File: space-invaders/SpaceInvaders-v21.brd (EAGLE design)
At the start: 91.4 x 91.4 mm, 27 parts, among them J2-J4 TM4C123GXL, J3-J1 TM4C123GXL, J5 NOKIA_5110, J6 NOKIA_5110, J7 9V, U1 LM7805CT

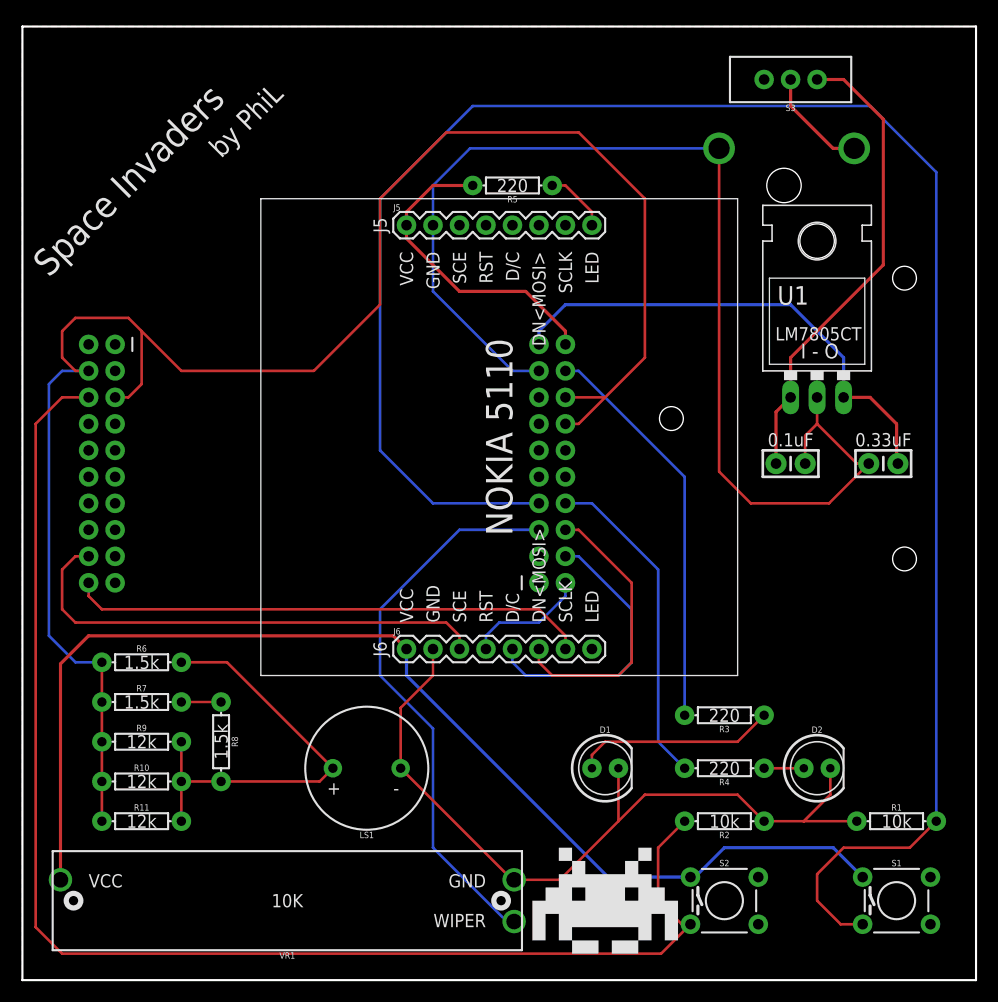
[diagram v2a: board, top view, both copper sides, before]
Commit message: Fillet corners of the boards
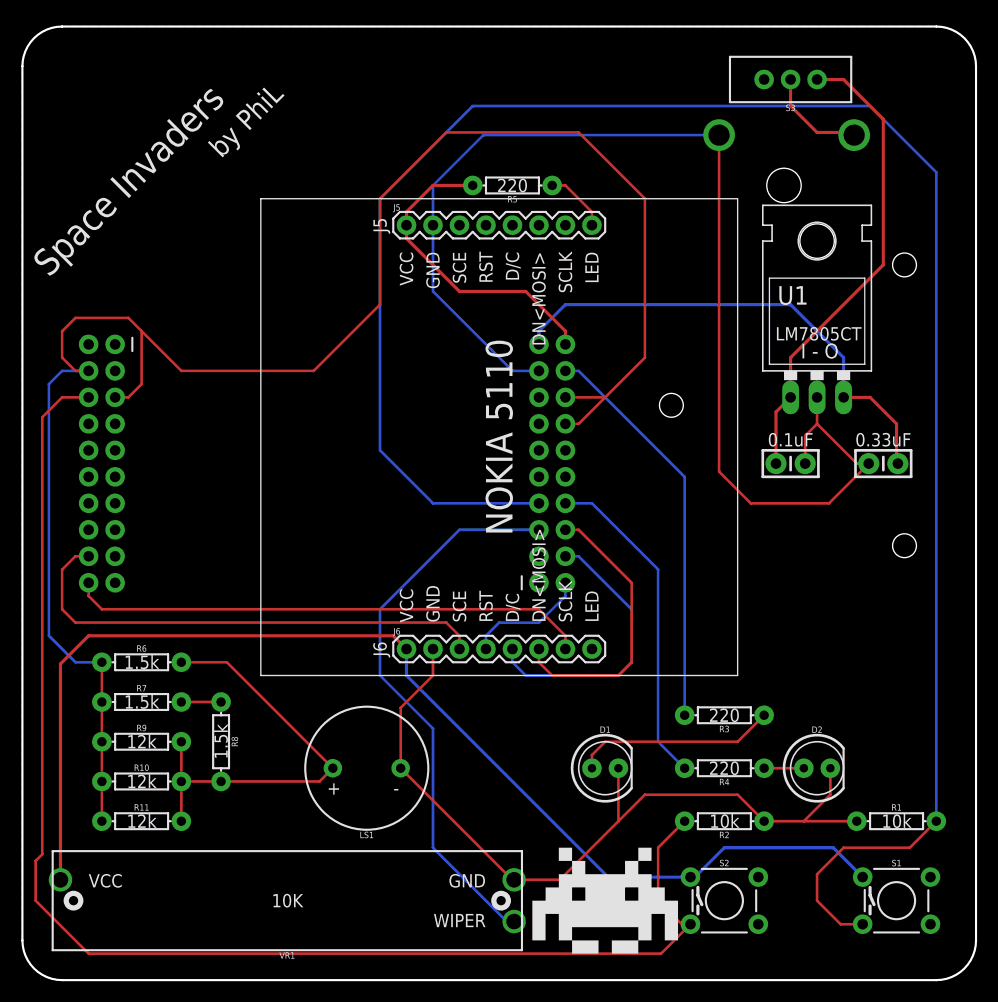
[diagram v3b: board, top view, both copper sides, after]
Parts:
- moved J7 1.27 mm to (58.4, 27.9)
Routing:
- net GND: track 190.4 -> 192.2 mm
- net PE0: track 132.1 -> 130.6 mm
- net VIN: track 10.3 -> 9.79 mm
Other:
- outline, holes or cut-outs redrawn
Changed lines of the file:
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@@
 <board>
 <plain>
-<wire x1="0" y1="0" x2="0" y2="91.44" width="0.2032" layer="20"/>
-<wire x1="0" y1="91.44" x2="91.44" y2="91.44" width="0.2032" layer="20"/>
-<wire x1="91.44" y1="91.44" x2="91.44" y2="0" width="0.2032" layer="20"/>
-<wire x1="91.44" y1="0" x2="0" y2="0" width="0.2032" layer="20"/>
+<wire x1="0" y1="3.81" x2="0" y2="87.63" width="0.2032" layer="20"/>
+<wire x1="3.81" y1="91.44" x2="87.63" y2="91.44" width="0.2032" layer="20"/>
+<wire x1="91.44" y1="87.63" x2="91.44" y2="3.81" width="0.2032" layer="20"/>
+<wire x1="87.63" y1="0" x2="3.81" y2="0" width="0.2032" layer="20"/>
 <wire x1="22.86" y1="74.93" x2="68.58" y2="74.93" width="0.127" layer="21"/>
 <wire x1="68.58" y1="74.93" x2="68.58" y2="29.21" width="0.127" layer="21"/>
@@
 <rectangle x1="52.705" y1="2.54" x2="53.975" y2="3.81" layer="21"/>
 <rectangle x1="51.435" y1="3.81" x2="52.705" y2="5.08" layer="21"/>
+<wire x1="0" y1="87.63" x2="3.81" y2="91.44" width="0.2032" layer="20" curve="-90"/>
+<wire x1="87.63" y1="91.44" x2="91.44" y2="87.63" width="0.2032" layer="20" curve="-90"/>
+<wire x1="91.44" y1="3.81" x2="87.63" y2="0" width="0.2032" layer="20" curve="-90"/>
+<wire x1="0" y1="3.81" x2="3.81" y2="0" width="0.2032" layer="20" curve="90"/>
 </plain>
 <attributes>
@@
 <attribute name="PROD_ID" value="CONN-08438" x="36.83" y="31.75" size="1.778" layer="27" display="off"/>
 </element>
-<element name="J7" library="SparkFun-Connectors" package="BC9VPC" value="9V" x="58.42" y="26.67" rot="MR90">
-<attribute name="PROD_ID" value="BATT-10855" x="58.42" y="26.67" size="1.778" layer="28" rot="MR90" display="off"/>
+<element name="J7" library="SparkFun-Connectors" package="BC9VPC" value="9V" x="58.42" y="27.94" rot="MR90">
+<attribute name="PROD_ID" value="BATT-10855" x="58.42" y="27.94" size="1.778" layer="28" rot="MR90" display="off"/>
 </element>
 <element name="LS1" library="SparkFun-Electromechanical" package="BUZZER-12MM" value="BUZZER" x="33.02" y="20.32" rot="R180">
@@
 <wire x1="47.15" y1="9.62" x2="46.97" y2="9.62" width="0.254" layer="1"/>
 <wire x1="46.97" y1="9.62" x2="36.27" y2="20.32" width="0.254" layer="1"/>
-<wire x1="66.802" y1="79.756" x2="42.926" y2="79.756" width="0.254" layer="16"/>
-<wire x1="42.926" y1="79.756" x2="39.37" y2="76.2" width="0.254" layer="16"/>
-<wire x1="39.37" y1="76.2" x2="39.37" y2="72.39" width="0.254" layer="16"/>
+<wire x1="39.37" y1="72.39" x2="39.37" y2="76.2" width="0.254" layer="16"/>
 <wire x1="39.37" y1="72.39" x2="39.37" y2="66.04" width="0.254" layer="16"/>
 <wire x1="39.37" y1="66.04" x2="46.99" y2="58.42" width="0.254" layer="16"/>
@@
 <wire x1="39.37" y1="29.21" x2="39.37" y2="31.75" width="0.254" layer="1"/>
 <wire x1="36.27" y1="20.32" x2="36.27" y2="26.11" width="0.254" layer="1"/>
-<wire x1="66.802" y1="79.756" x2="66.802" y2="48.768" width="0.254" layer="1"/>
+<wire x1="66.802" y1="81.026" x2="66.802" y2="48.768" width="0.254" layer="1"/>
 <wire x1="66.802" y1="48.768" x2="69.85" y2="45.72" width="0.254" layer="1"/>
 <wire x1="69.85" y1="45.72" x2="77.343" y2="45.72" width="0.254" layer="1"/>
 <wire x1="77.343" y1="45.72" x2="81.153" y2="49.53" width="0.254" layer="1"/>
+<wire x1="44.196" y1="81.026" x2="66.802" y2="81.026" width="0.254" layer="16"/>
+<wire x1="39.37" y1="76.2" x2="44.196" y2="81.026" width="0.254" layer="16"/>
+<wire x1="77.47" y1="20.32" x2="77.343" y2="45.72" width="0" layer="19" extent="1-1"/>
+<wire x1="6.35" y1="60.96" x2="39.37" y2="66.04" width="0" layer="19" extent="16-16"/>
 <polygon width="0.254" layer="1" isolate="0.3048">
-<vertex x="0" y="0"/>
-<vertex x="0" y="91.44"/>
-<vertex x="91.44" y="91.44"/>
-<vertex x="91.44" y="0"/>
+<vertex x="0" y="3.81"/>
+<vertex x="0" y="87.63" curve="-90"/>
+<vertex x="3.81" y="91.44"/>
+<vertex x="87.63" y="91.44" curve="-90"/>
+<vertex x="91.44" y="87.63"/>
+<vertex x="91.44" y="3.81" curve="-90"/>
+<vertex x="87.63" y="0"/>
+<vertex x="3.81" y="0" curve="-90"/>
 </polygon>
-<wire x1="6.35" y1="60.96" x2="39.37" y2="66.04" width="0" layer="19" extent="16-16"/>
 </signal>
 <signal name="VBUS" class="1">
@@
 <wire x1="60.96" y1="7.62" x2="60.96" y2="12.7" width="0.254" layer="1"/>
 <wire x1="60.96" y1="12.7" x2="63.5" y2="15.24" width="0.254" layer="1"/>
-<wire x1="6.35" y1="55.88" x2="3.81" y2="55.88" width="0.254" layer="1"/>
-<wire x1="3.81" y1="55.88" x2="1.27" y2="53.34" width="0.254" layer="1"/>
-<wire x1="1.27" y1="53.34" x2="1.27" y2="5.08" width="0.254" layer="1"/>
-<wire x1="1.27" y1="5.08" x2="3.81" y2="2.54" width="0.254" layer="1"/>
-<wire x1="3.81" y1="2.54" x2="61.2394" y2="2.54" width="0.254" layer="1"/>
-<wire x1="61.2394" y1="2.54" x2="64.0588" y2="5.3594" width="0.254" layer="1"/>
+<wire x1="64.0588" y1="5.3594" x2="61.2394" y2="2.54" width="0.254" layer="1"/>
+<wire x1="61.2394" y1="2.54" x2="6.35" y2="2.54" width="0.254" layer="1"/>
+<wire x1="6.35" y1="2.54" x2="1.27" y2="7.62" width="0.254" layer="1"/>
+<wire x1="1.27" y1="7.62" x2="1.27" y2="11.43" width="0.254" layer="1"/>
+<wire x1="1.27" y1="11.43" x2="1.905" y2="12.065" width="0.254" layer="1"/>
+<wire x1="1.905" y1="12.065" x2="1.905" y2="53.975" width="0.254" layer="1"/>
+<wire x1="1.905" y1="53.975" x2="3.81" y2="55.88" width="0.254" layer="1"/>
+<wire x1="3.81" y1="55.88" x2="6.35" y2="55.88" width="0.254" layer="1"/>
 </signal>
 <signal name="VIN" class="1">
 <contactref element="J7" pad="V+"/>
 <contactref element="S3" pad="2"/>
-<wire x1="79.756" y1="79.756" x2="77.724" y2="79.756" width="0.3048" layer="1"/>
-<wire x1="77.724" y1="79.756" x2="73.66" y2="83.82" width="0.3048" layer="1"/>
-<wire x1="73.66" y1="83.82" x2="73.66" y2="86.36" width="0.3048" layer="1"/>
+<wire x1="73.66" y1="86.36" x2="73.66" y2="83.82" width="0.3048" layer="1"/>
+<wire x1="73.66" y1="83.82" x2="76.2" y2="81.28" width="0.3048" layer="1"/>
+<wire x1="76.2" y1="81.28" x2="79.502" y2="81.28" width="0.3048" layer="1"/>
+<wire x1="79.502" y1="81.28" x2="79.756" y2="81.026" width="0.3048" layer="1"/>
 </signal>
 </signals>

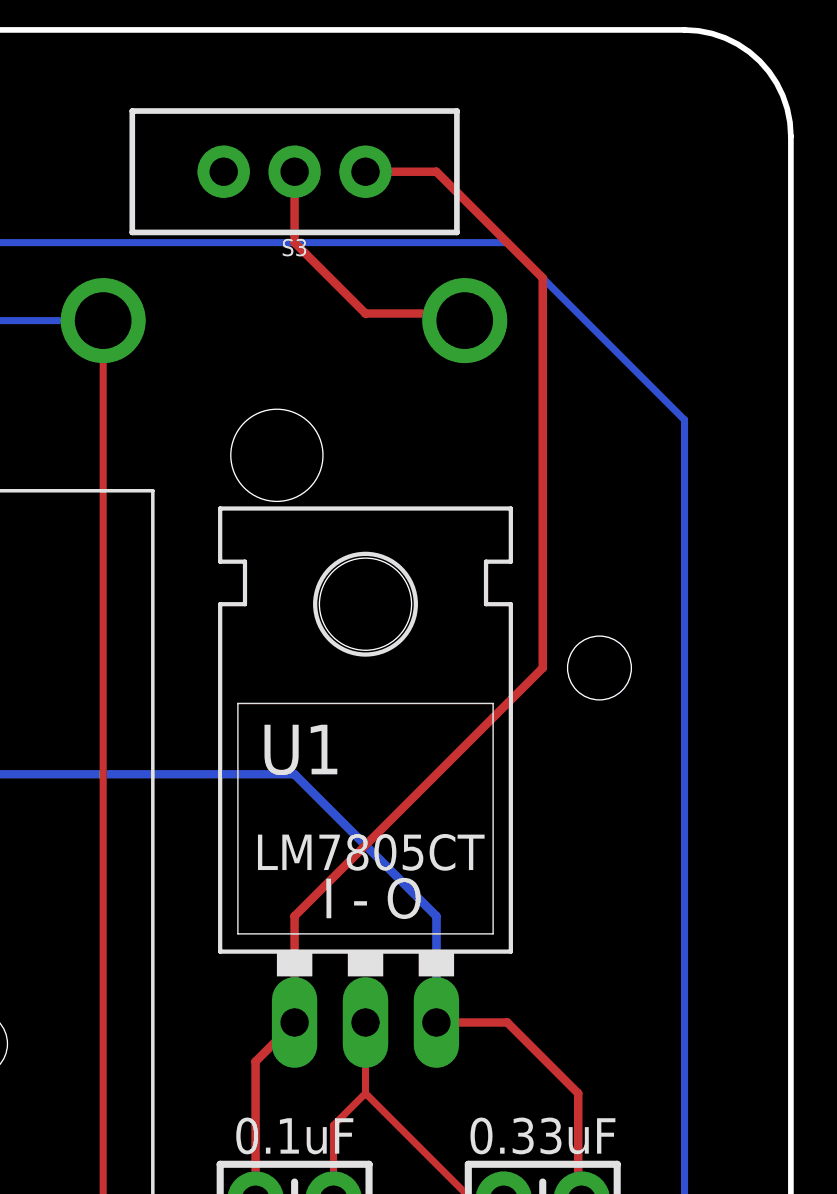
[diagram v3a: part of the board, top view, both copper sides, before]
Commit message: Change pin position SPDT slide switch
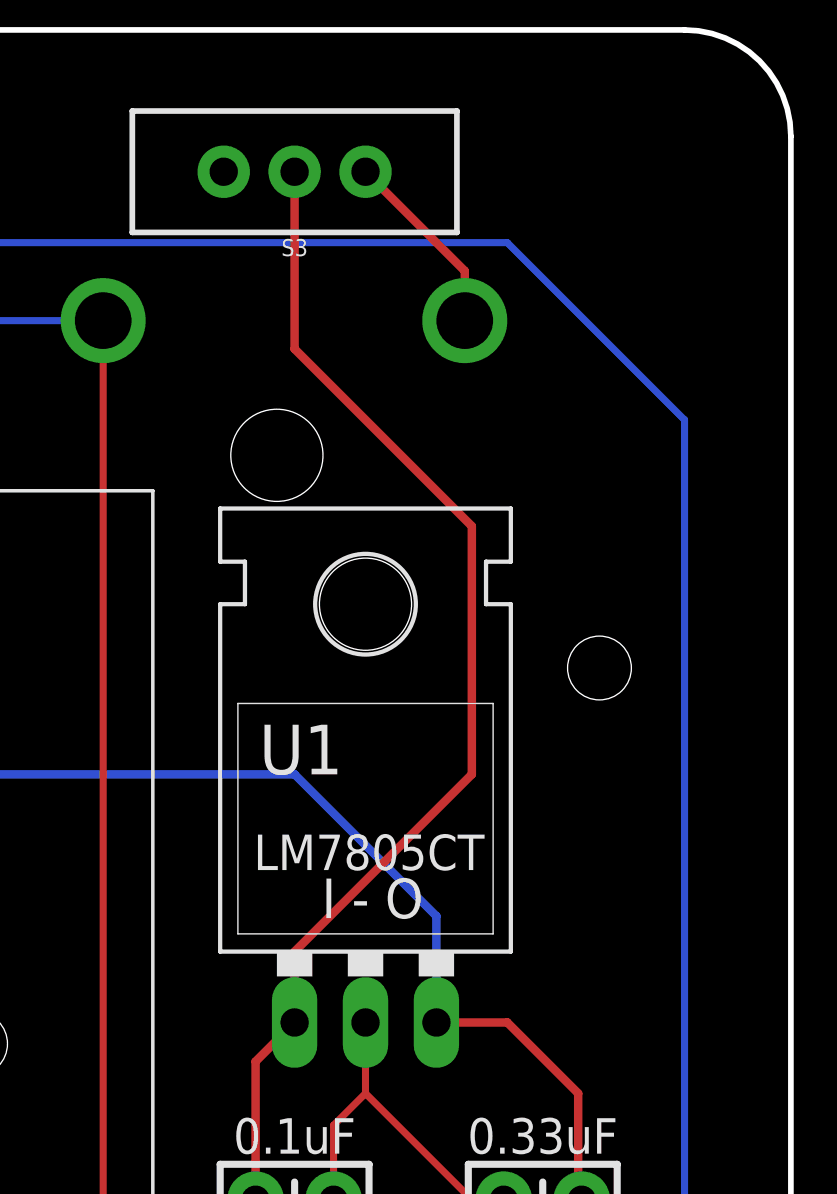
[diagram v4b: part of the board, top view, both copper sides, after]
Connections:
- net 9V: now also J7.V+; no longer C2.1, U1.IN
- net VIN: now also C2.1, U1.IN; no longer J7.V+
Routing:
- net 9V: track 45.2 -> 6.81 mm
- net VIN: track 9.79 -> 42.7 mm
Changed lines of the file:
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@@
 <wire x1="28.5" y1="19.05" x2="29.77" y2="20.32" width="0.254" layer="1"/>
 </signal>
-<signal name="9V" class="1">
+<signal name="VIN" class="1">
 <contactref element="U1" pad="IN"/>
 <contactref element="C2" pad="1"/>
 <wire x1="72.263" y1="49.53" x2="72.263" y2="54.483" width="0.3048" layer="1"/>
 <wire x1="73.66" y1="55.88" x2="72.263" y2="54.483" width="0.3048" layer="1"/>
-<contactref element="S3" pad="3"/>
-<wire x1="76.2" y1="86.36" x2="78.74" y2="86.36" width="0.3048" layer="1"/>
-<wire x1="78.74" y1="86.36" x2="82.55" y2="82.55" width="0.3048" layer="1"/>
-<wire x1="82.55" y1="82.55" x2="82.55" y2="68.58" width="0.3048" layer="1"/>
-<wire x1="82.55" y1="68.58" x2="73.66" y2="59.69" width="0.3048" layer="1"/>
-<wire x1="73.66" y1="59.69" x2="73.66" y2="55.88" width="0.3048" layer="1"/>
+<wire x1="73.66" y1="58.42" x2="73.66" y2="55.88" width="0.3048" layer="1"/>
+<contactref element="S3" pad="2"/>
+<wire x1="73.66" y1="86.36" x2="73.66" y2="80.01" width="0.3048" layer="1"/>
+<wire x1="73.66" y1="80.01" x2="80.01" y2="73.66" width="0.3048" layer="1"/>
+<wire x1="80.01" y1="73.66" x2="80.01" y2="64.77" width="0.3048" layer="1"/>
+<wire x1="80.01" y1="64.77" x2="73.66" y2="58.42" width="0.3048" layer="1"/>
 </signal>
 <signal name="GND" airwireshidden="yes">
@@
 <wire x1="3.81" y1="55.88" x2="6.35" y2="55.88" width="0.254" layer="1"/>
 </signal>
-<signal name="VIN" class="1">
+<signal name="9V" class="1">
 <contactref element="J7" pad="V+"/>
-<contactref element="S3" pad="2"/>
-<wire x1="73.66" y1="86.36" x2="73.66" y2="83.82" width="0.3048" layer="1"/>
-<wire x1="73.66" y1="83.82" x2="76.2" y2="81.28" width="0.3048" layer="1"/>
-<wire x1="76.2" y1="81.28" x2="79.502" y2="81.28" width="0.3048" layer="1"/>
-<wire x1="79.502" y1="81.28" x2="79.756" y2="81.026" width="0.3048" layer="1"/>
+<contactref element="S3" pad="3"/>
+<wire x1="79.756" y1="81.026" x2="79.756" y2="82.804" width="0.3048" layer="1"/>
+<wire x1="79.756" y1="82.804" x2="76.2" y2="86.36" width="0.3048" layer="1"/>
 </signal>
 </signals>

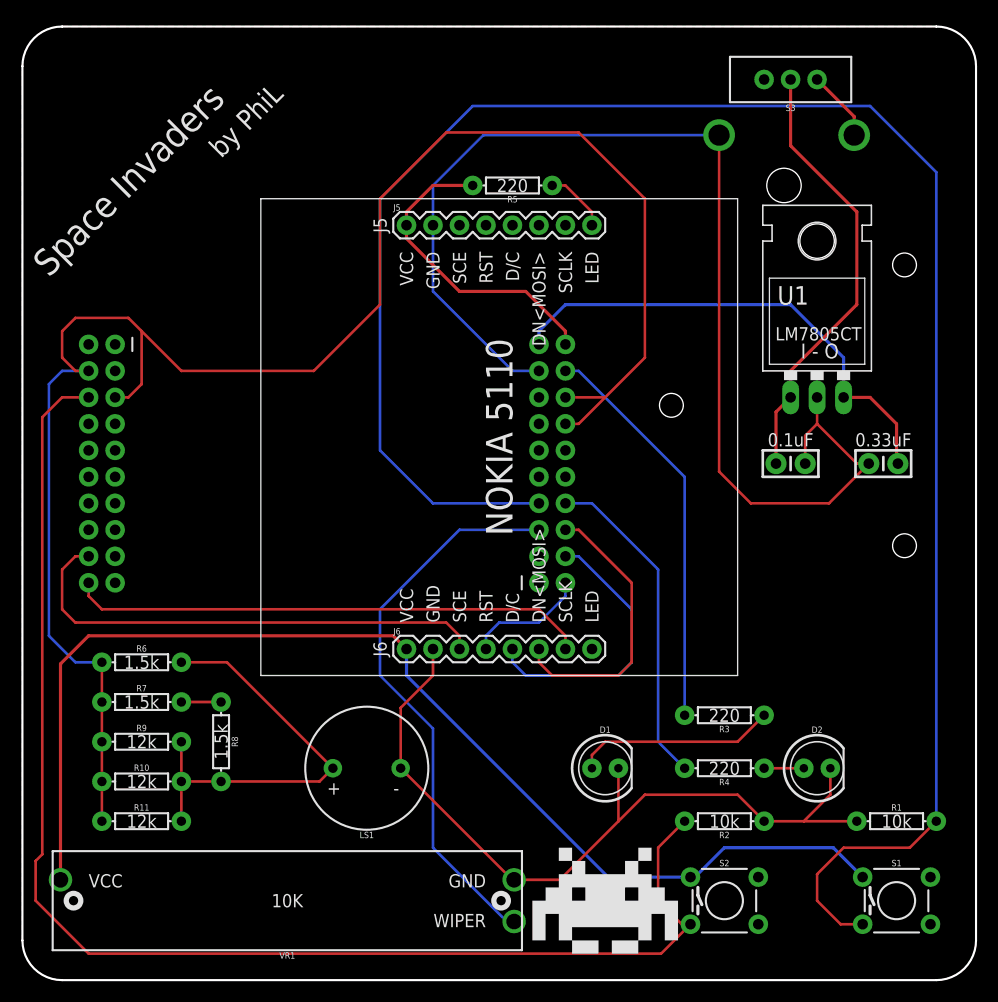
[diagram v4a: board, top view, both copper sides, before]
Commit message: Add GND to RATSNEST
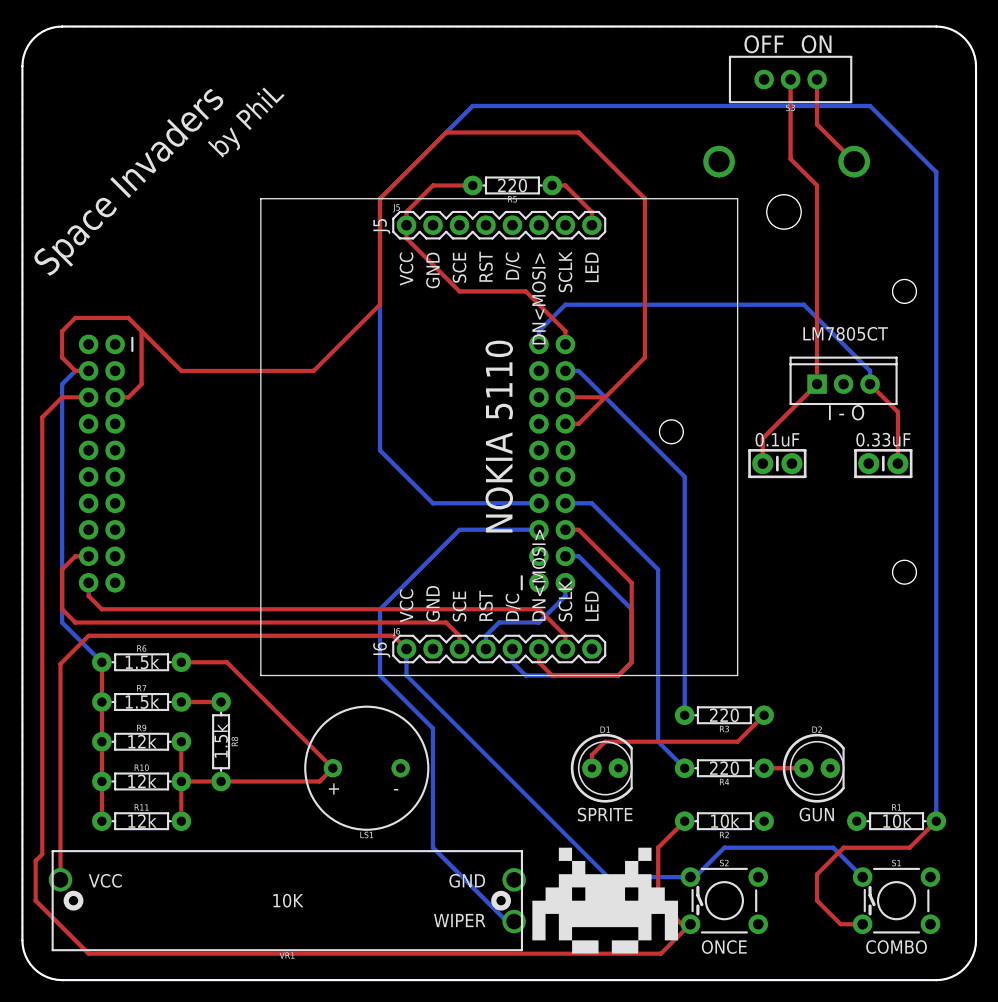
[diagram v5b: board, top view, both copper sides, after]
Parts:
- D1: value RED -> RED_SPRITES
- D2: value YELLOW -> YELLOW_GUN
- S1: value SPECIAL -> ONCE
- S2: value REGULAR -> COMBO
- U1: device SparkFun-IC-Power:TO-220-ALT -> SparkFun-IC-Power:TO220-IGO
- moved U1 3.59 mm to (78.7, 57.1)
- moved J7 2.54 mm to (58.4, 25.4)
- moved C2 1.27 mm to (72.4, 49.5)
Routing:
- net GND: track 192.2 -> 0.00 mm
- net DAC: track 169.5 -> 166.2 mm
- net VIN: track 42.7 -> 40.0 mm
- net 9V: track 6.81 -> 9.35 mm
- net VBUS: track 47.4 -> 46.7 mm
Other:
- board text added: "COMBO"
- board text added: "GUN"
- board text added: "OFF"
- board text added: "ON"
- board text added: "ONCE"
- board text added: "SPRITE"
